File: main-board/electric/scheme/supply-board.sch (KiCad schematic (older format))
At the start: 141 parts, among them K1 CONN_3, P1 PWR-IN, P10 TST, P11 TST, P12 PWR-IN, P13 CONN_4, P14 PWR-IN, P16 TST, P2 PWR-IN, P3 CONN_4, P4 cross board conn, P5 PWR-IN, P6 TST, P7 TST, P8 TST, P9 CONN_3X2, Q1 BC847, Q10 IRLML2502, Q11 IRLML2244, Q12 IRLML2244, Q2 BC847, Q3 BC847, Q4 IRLML2244, Q5 BC847, Q6 BC857, Q7 BC847, Q8 BC857, Q9 BC847, U1 NCP3063, U2 L293, U3 MINI-USB-B, X1 8MHz

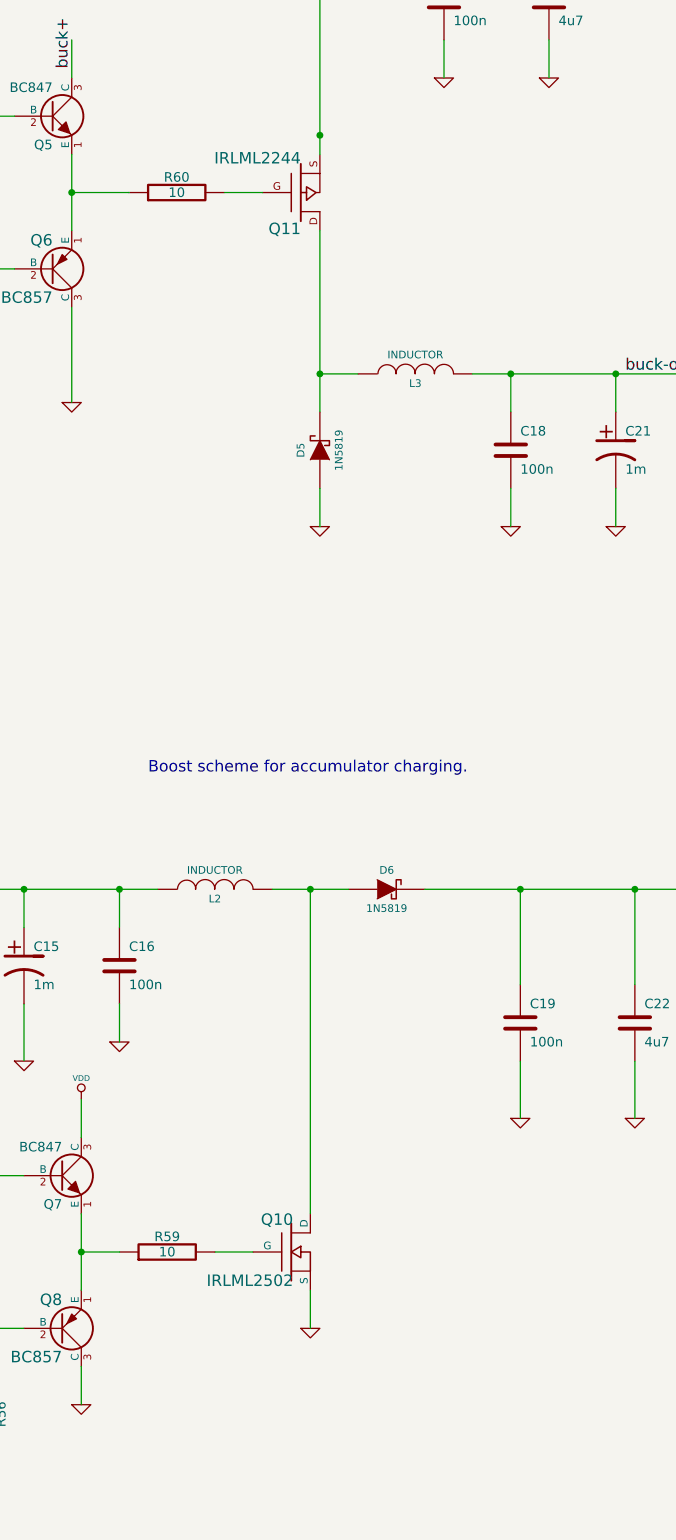
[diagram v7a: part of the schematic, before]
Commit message: For boost and buck circuits made optional sot23/sot223 transistor packages.
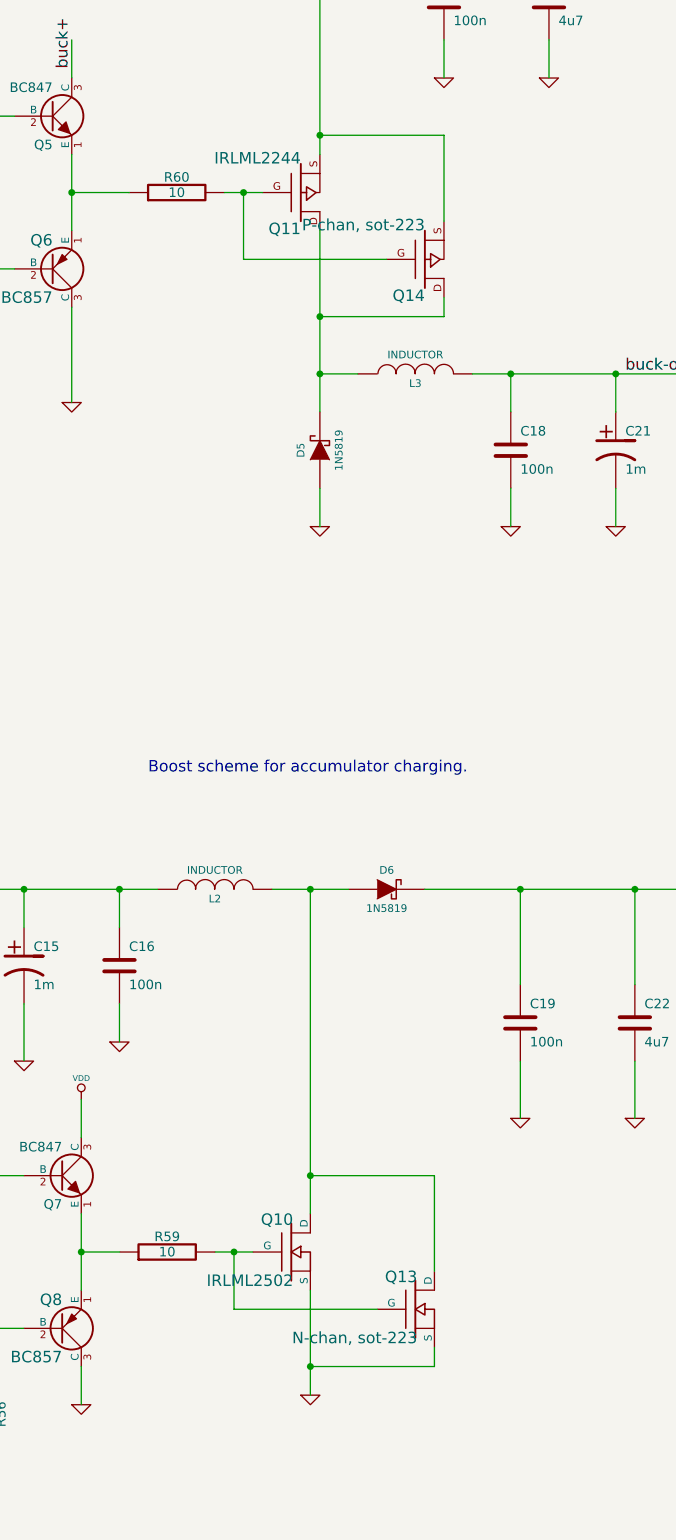
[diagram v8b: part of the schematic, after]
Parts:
- added Q13: N-chan, sot-223, symbol MOS_N
- added Q14: P-chan, sot-223, symbol MOS_P
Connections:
- wire segments 430 -> 442
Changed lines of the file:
@@
 L GND #PWR038
 U 1 1 520E86AB
-P 26250 8900
-F 0 "#PWR038" H 26250 8900 30  0001 C CNN
-F 1 "GND" H 26250 8830 30  0001 C CNN
-F 2 "" H 26250 8900 60  0001 C CNN
-F 3 "" H 26250 8900 60  0001 C CNN
-	1    26250 8900
+P 26250 9250
+F 0 "#PWR038" H 26250 9250 30  0001 C CNN
+F 1 "GND" H 26250 9180 30  0001 C CNN
+F 2 "" H 26250 9250 60  0001 C CNN
+F 3 "" H 26250 9250 60  0001 C CNN
+	1    26250 9250
 	1    0    0    -1
 $EndComp
@@
 	25250 8500 25050 8500
 Wire Wire Line
-	26250 8700 26250 8900
+	26250 8700 26250 9250
 Connection ~ 25250 6600
 Wire Wire Line
@@
 scl-int
 NoConn ~ 14300 9350
+$Comp
+L MOS_P Q14
+U 1 1 522F80F1
+P 26850 3300
+F 0 "Q14" H 26850 3490 60  0000 R CNN
+F 1 "P-chan, sot-223" H 26850 3120 60  0000 R CNN
+F 2 "" H 26850 3300 60  0001 C CNN
+F 3 "" H 26850 3300 60  0001 C CNN
+	1    26850 3300
+	1    0    0    1
+$EndComp
+Wire Wire Line
+	26650 3300 25900 3300
+Wire Wire Line
+	25900 3300 25900 2950
+Connection ~ 25900 2950
+Wire Wire Line
+	26950 3500 26950 3600
+Wire Wire Line
+	26950 3600 26300 3600
+Connection ~ 26300 3600
+Wire Wire Line
+	26950 3100 26950 2650
+Wire Wire Line
+	26950 2650 26300 2650
+$Comp
+L MOS_N Q13
+U 1 1 522F8723
+P 26800 8800
+F 0 "Q13" H 26810 8970 60  0000 R CNN
+F 1 "N-chan, sot-223" H 26810 8650 60  0000 R CNN
+F 2 "" H 26800 8800 60  0001 C CNN
+F 3 "" H 26800 8800 60  0001 C CNN
+	1    26800 8800
+	1    0    0    -1
+$EndComp
+Wire Wire Line
+	26900 8600 26900 8100
+Wire Wire Line
+	26900 8100 26250 8100
+Connection ~ 26250 8100
+Wire Wire Line
+	26900 9000 26900 9100
+Wire Wire Line
+	26900 9100 26250 9100
+Connection ~ 26250 9100
+Wire Wire Line
+	26600 8800 25850 8800
+Wire Wire Line
+	25850 8800 25850 8500
+Connection ~ 25850 8500
 $EndSCHEMATC
